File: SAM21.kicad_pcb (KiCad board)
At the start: 2 copper layers, 122 parts, among them J1 629105150521, J2 Conn_ARM_JTAG_SWD_10, J3 Conn_01x02_Male, J4 Conn_01x04_Male, J5 Conn_01x04_Male, J6 Conn_01x04_Male, J7 Conn_01x04_Male, J8 Conn_01x04_Male, Q1 BSS138, Q10 BSS138, Q2 BSS138, Q5 BSS138, Q6 BSS138, Q8 BSS138, SW1 SW_Push, SW2 SW_Push, U1 ATSAMD21G18A-MU, U2 AP1117-33, U3 ESD5V3U2U-03F, U4 74lvc244, U5 XBEE, U7 XBEE, U9 ATECC608A-MAHDA, Y1 32.768kHz

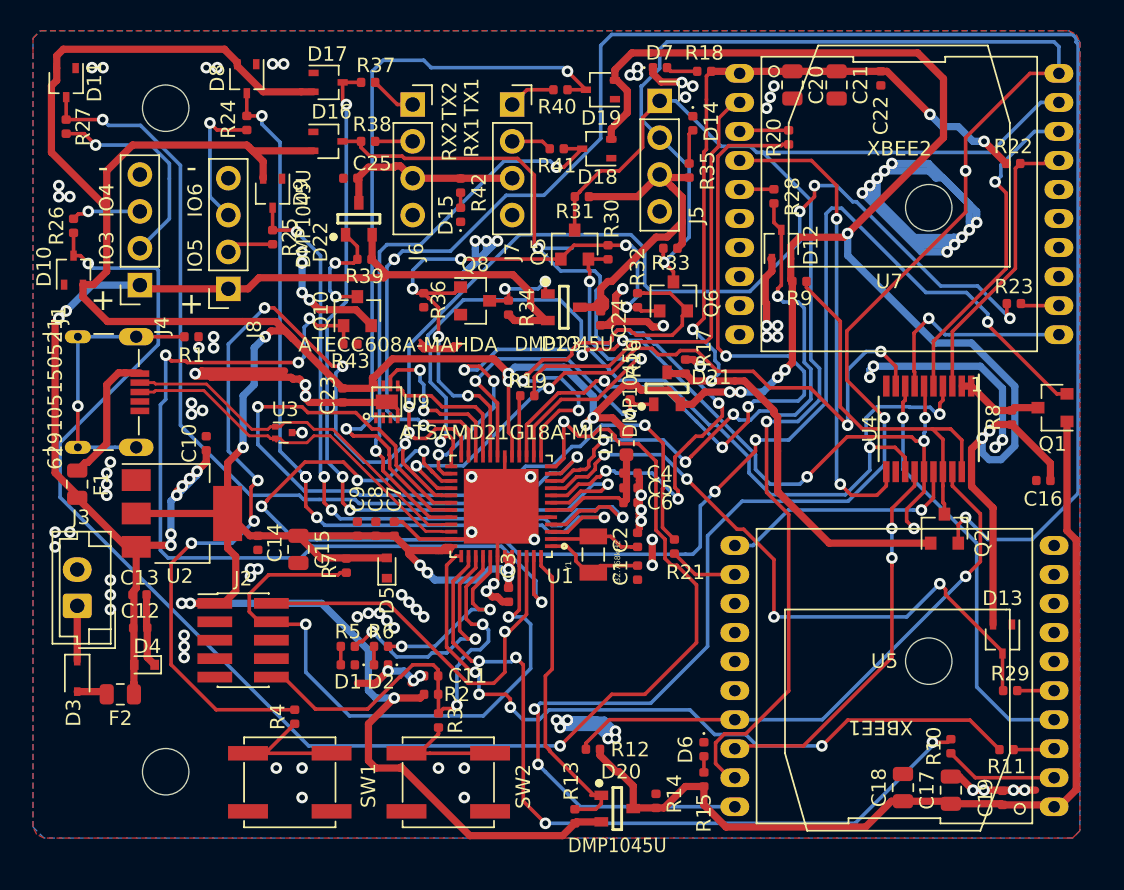
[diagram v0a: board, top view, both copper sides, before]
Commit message: Fixed One Exception
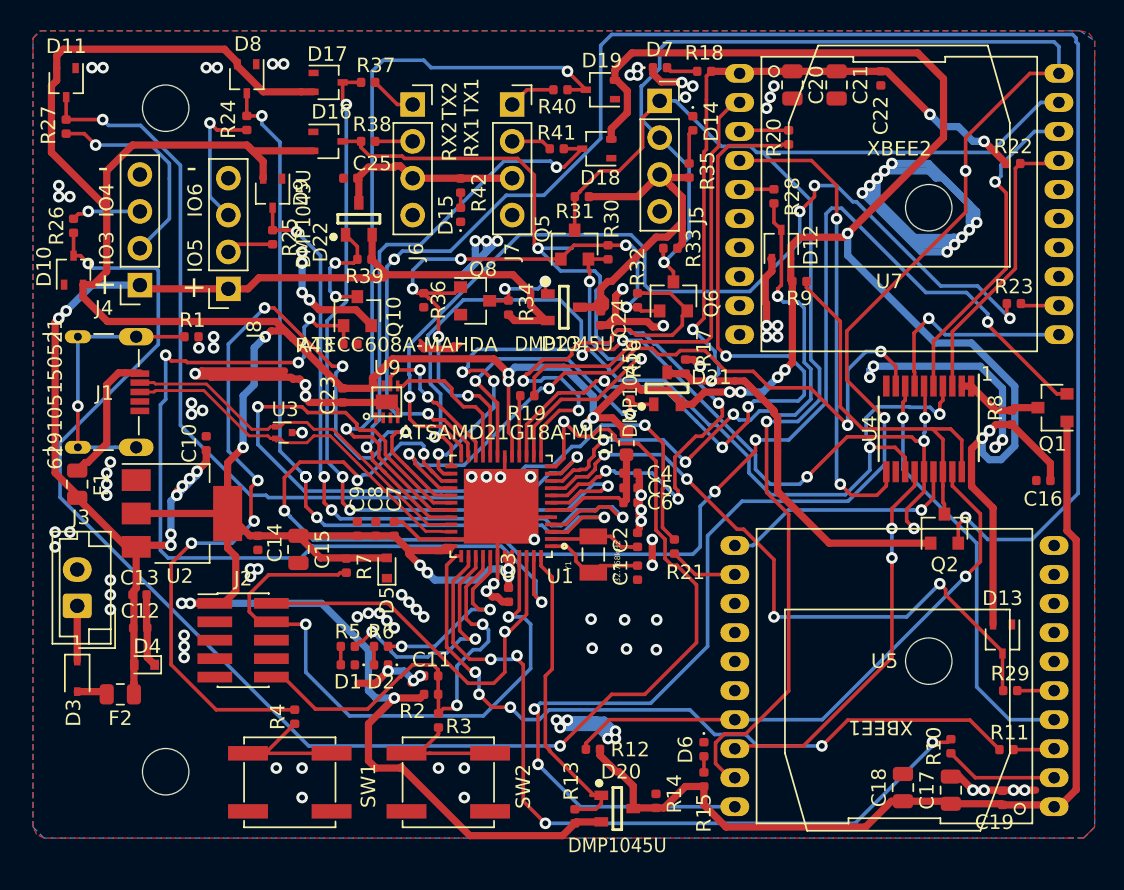
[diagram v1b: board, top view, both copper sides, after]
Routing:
- net D0_SW: track 64.4 -> 66.5 mm
- net D21_MISO2.3A: track 48.0 -> 49.8 mm
- net D18_SCL_IMU4.3B: track 12.1 -> 10.5 mm
- net D29_INT_XB22.4D: track 68.9 -> 67.4 mm, vias 5 -> 4
- net D23_CS_XB12.2A: track 99.6 -> 98.5 mm
- net D28_CS_XB22.2C: track 119.2 -> 118.2 mm
- net D19_MOSI2.2A: track 65.5 -> 64.7 mm
- net D24_INT_XB12.4B: track 59.4 -> 58.6 mm
- net D20_SCK2.2A: track 61.5 -> 62.0 mm
- net GND: vias 111 -> 118
